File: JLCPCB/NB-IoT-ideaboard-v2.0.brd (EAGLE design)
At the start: 93 x 65 mm, 117 parts, among them Q1 32.768kHz, Q2 9013, Q3 9013, Q4 9013, Q5 9013, U1 STM32F103RBT6, U2 MCP73831T-2ACI/OT, U3 AP2112-3.3, U4 PAM2401, U5 MICROSIM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

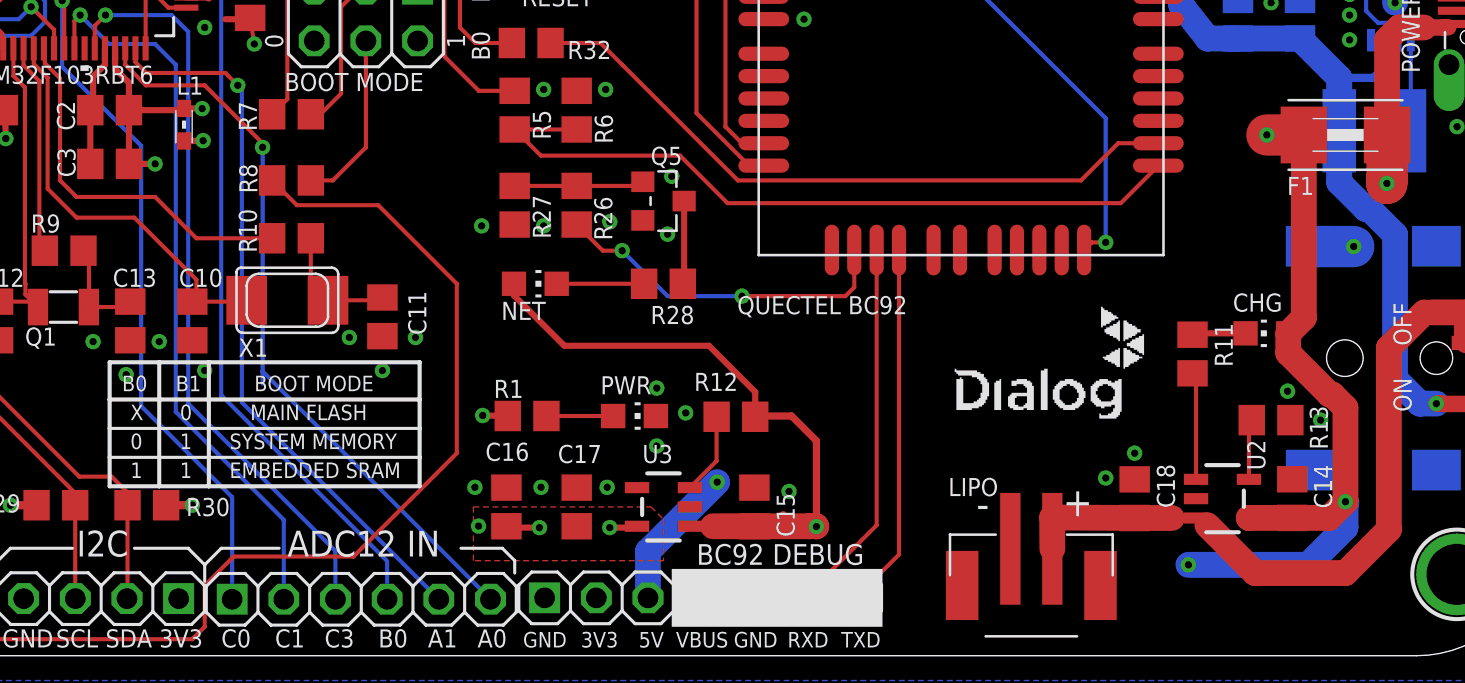
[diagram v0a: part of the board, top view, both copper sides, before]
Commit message: JLCPCB LED placements changed
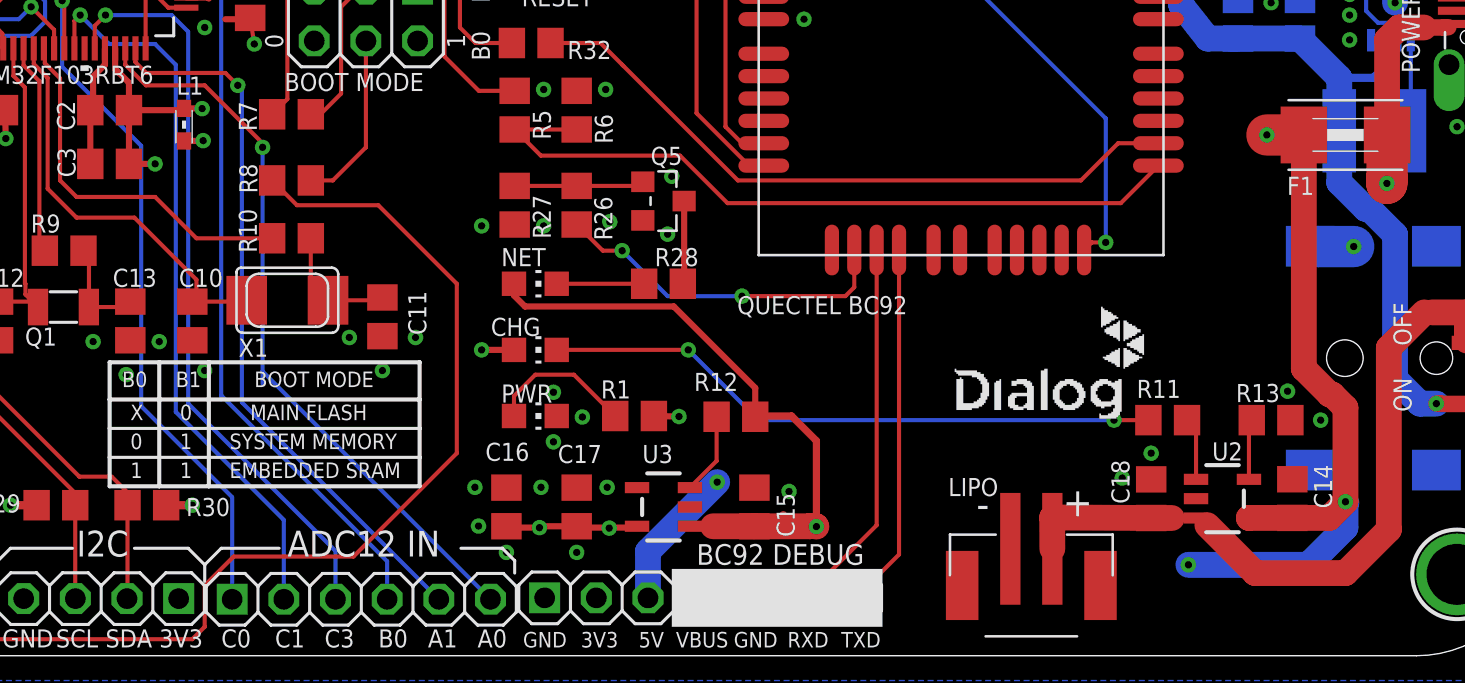
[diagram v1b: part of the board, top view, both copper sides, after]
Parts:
- moved CHG 36.0 mm to (63.0, 52.2), turned to 270 degrees
- moved R1 5.28 mm to (67.9, 49.0), turned to 0 degrees
- moved PWR 4.88 mm to (63.0, 49.0)
- moved R11 3.47 mm to (94.1, 48.8), turned to 180 degrees
- moved C18 0.81 mm to (93.3, 44.9)
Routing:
- net N$9: track 2.63 -> 30.5 mm, vias 0 -> 2
- net VBUS: track 135.6 -> 160.1 mm, vias 3 -> 4
- net N$3: track 3.28 -> 7.24 mm
- net N$11: track 5.28 -> 3.09 mm
- net +3V3: track 43.3 -> 43.4 mm, vias 15 -> 17
- removed copper zone on layer 1, net +3V3

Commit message: JLCPCB header position changes
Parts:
- removed R31: 1k5, rcl:R0805
- added JP4: (no value), jumper:JP1
- added POWER-PINS1: (no value), pinhead-2:1X04-S
- moved S1 0.61 mm to (110.5, 52.4)
- moved L2 0.41 mm to (103.8, 63.0)
- moved ANALOG 0.41 mm to (54.8, 40.0)
- moved I2C1 0.41 mm to (42.1, 40.0)
- moved JP1 0.41 mm to (76.6, 40.0)
- moved POWER-PINS 0.41 mm to (67.7, 40.0)
- moved U4 0.20 mm to (104.9, 69.7)
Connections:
- removed net USB_D_P: R31.2
- new net N$24: JP4.2, S1.1, S1.2
- net +3V3: now also POWER-PINS1.2, SWD.3; no longer R31.1, SWD.6
- net +4.1V: now also JP4.1; no longer S1.1, S1.2
- net +5V: now also POWER-PINS1.3
- net GND: now also POWER-PINS1.1, SWD.5; no longer SWD.4
- net JTCK/SWCLK: now also SWD.4; no longer SWD.5
- net JTMS/SWDIO: now also SWD.6; no longer SWD.3
- net VBUS: now also POWER-PINS1.4
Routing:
- net +5V: track 62.8 -> 100.0 mm, vias 2 -> 4
- net VBUS: track 160.1 -> 193.5 mm
- net N$24: track 0.00 -> 21.2 mm
- net +4.1V: track 35.1 -> 14.6 mm
- net JTMS/SWDIO: track 19.2 -> 16.9 mm, vias 1 -> 0
- net +3V3: track 43.4 -> 42.1 mm, vias 17 -> 16
- net JTCK/SWCLK: track 12.6 -> 13.6 mm, vias 0 -> 1
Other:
- board text added: "5V INPUT"
- board text added: "5V STEP UP CONVERTER SOLDER IF NEEDED"
- board text added: "CAN"
- board text added: "I2C 1"
- board text added: "JP1"
- board text added: "USR"
- board text removed: "CAN1"
- board text removed: "I2C"
- board text removed: "LED"
- board text removed: "check antenna"
- board text removed: "need 5V pins"
